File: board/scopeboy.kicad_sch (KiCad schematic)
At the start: 110 parts, among them J1 USB_C_Receptacle_USB2.0_16P, J2 SM03B-SRSS-TB, J3 SM03B-SRSS-TB, J4 Conn_01x10, J5 SM04B-SRSS-TB, J6 HDMI_A, J8 Conn_01x02, J9 Conn_01x08, SW1 SW_Push, SW2 SW_Push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

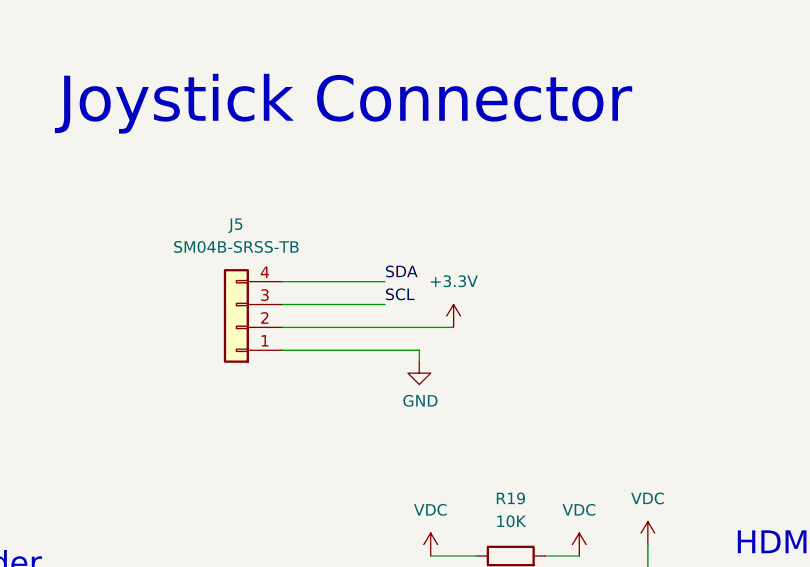
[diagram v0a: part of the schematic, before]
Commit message: Fixed joystick qwiic connector bug
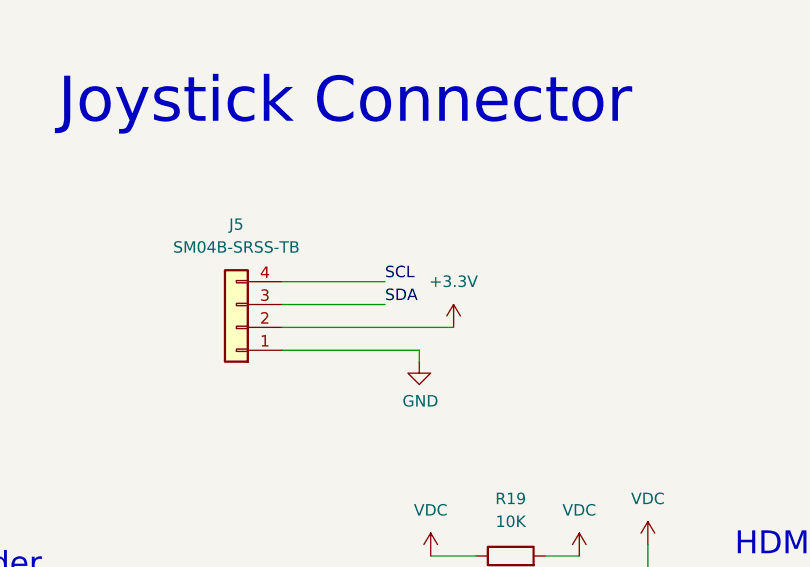
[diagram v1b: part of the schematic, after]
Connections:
- net SCL: now also J5.4 (Pin_4); no longer J5.3 (Pin_3)
- net SDA: now also J5.3 (Pin_3); no longer J5.4 (Pin_4)
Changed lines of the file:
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@@
 	(title_block
 		(title "Scopeboy")
-		(date "2026-05-12")
+		(date "2026-05-13")
 		(rev "V1.1")
 		(company "Cornell University Electrical and Computer Engineering")
@@
 		)
 	)
-	(label "SDA"
-		(at 478.79 49.53 0)
+	(label "HDMI_CKP"
+		(at 551.18 107.95 0)
 		(effects
 			(font
@@
 		)
 	)
-	(label "HDMI_CKP"
-		(at 551.18 107.95 0)
+	(label "GPIO0"
+		(at 18.415 116.205 0)
 		(effects
 			(font
@@
 		)
 	)
-	(label "GPIO0"
-		(at 18.415 116.205 0)
+	(label "SDA"
+		(at 478.79 52.07 0)
 		(effects
 			(font
@@
 		)
 	)
+	(label "SCL"
+		(at 478.79 49.53 0)
+		(effects
+			(font
+				(size 1.27 1.27)
+			)
+			(justify left bottom)
+		)
+	)
 	(label "HDMI_D2P"
 		(at 250.19 142.24 180)
@@
 		)
 	)
-	(label "SCL"
-		(at 478.79 52.07 0)
-		(effects
-			(font
-				(size 1.27 1.27)
-			)
-			(justify left bottom)
-		)
-	)

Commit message: Started work on fixing PCB bugs
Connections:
- net GPIO31 is gone; now on net PowerStatus: U4.39 (GPIO31)
- net PowerStatus: no longer U4.4 (GPIO7)
- net CLK renamed ADC_CLK
- net ADC_CLK: now also U4.4 (GPIO7)
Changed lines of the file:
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@@
 	(title_block
 		(title "Scopeboy")
-		(date "2026-05-13")
+		(date "2026-05-12")
 		(rev "V1.1")
 		(company "Cornell University Electrical and Computer Engineering")
@@
 		)
 	)
-	(label "MISO"
-		(at 410.21 39.37 0)
+	(label "PowerStatus"
+		(at 250.19 190.5 180)
 		(effects
 			(font
 				(size 1.27 1.27)
 			)
-			(justify left bottom)
+			(justify right bottom)
 		)
 	)
-	(label "USB_D+"
-		(at 267.97 95.25 180)
+	(label "MISO"
+		(at 410.21 39.37 0)
 		(effects
 			(font
 				(size 1.27 1.27)
 			)
-			(justify right bottom)
+			(justify left bottom)
 		)
 	)
-	(label "PowerStatus"
-		(at 250.19 129.54 180)
+	(label "USB_D+"
+		(at 267.97 95.25 180)
 		(effects
 			(font
@@
 		)
 	)
-	(label "GPIO31"
-		(at 250.19 190.5 180)
-		(effects
-			(font
-				(size 1.27 1.27)
-			)
-			(justify right bottom)
-		)
-	)
 	(label "USB_D-"
 		(at 267.97 104.14 180)
@@
 		)
 	)
+	(label "ADC_CLK"
+		(at 250.19 129.54 180)
+		(effects
+			(font
+				(size 1.27 1.27)
+			)
+			(justify right bottom)
+		)
+	)
 	(label "D3"
 		(at 250.19 200.66 180)
@@
 		)
 	)
-	(global_label "CLK"
-		(shape input)
+	(label "ADC_CLK"
 		(at 496.57 331.47 0)
-		(fields_autoplaced yes)
 		(effects
 			(font
 				(size 1.27 1.27)
 			)
-			(justify left)
-		)
-		(property "Intersheetrefs" "${INTERSHEET_REFS}"
-			(at 502.4691 331.47 0)
-			(hide yes)
-			(show_name no)
-			(do_not_autoplace no)
-			(effects
-				(font
-					(size 1.27 1.27)
-				)
-				(justify left)
-			)
+			(justify left bottom)
 		)
 	)
